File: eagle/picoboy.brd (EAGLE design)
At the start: 72 x 114.5 mm, 9 parts

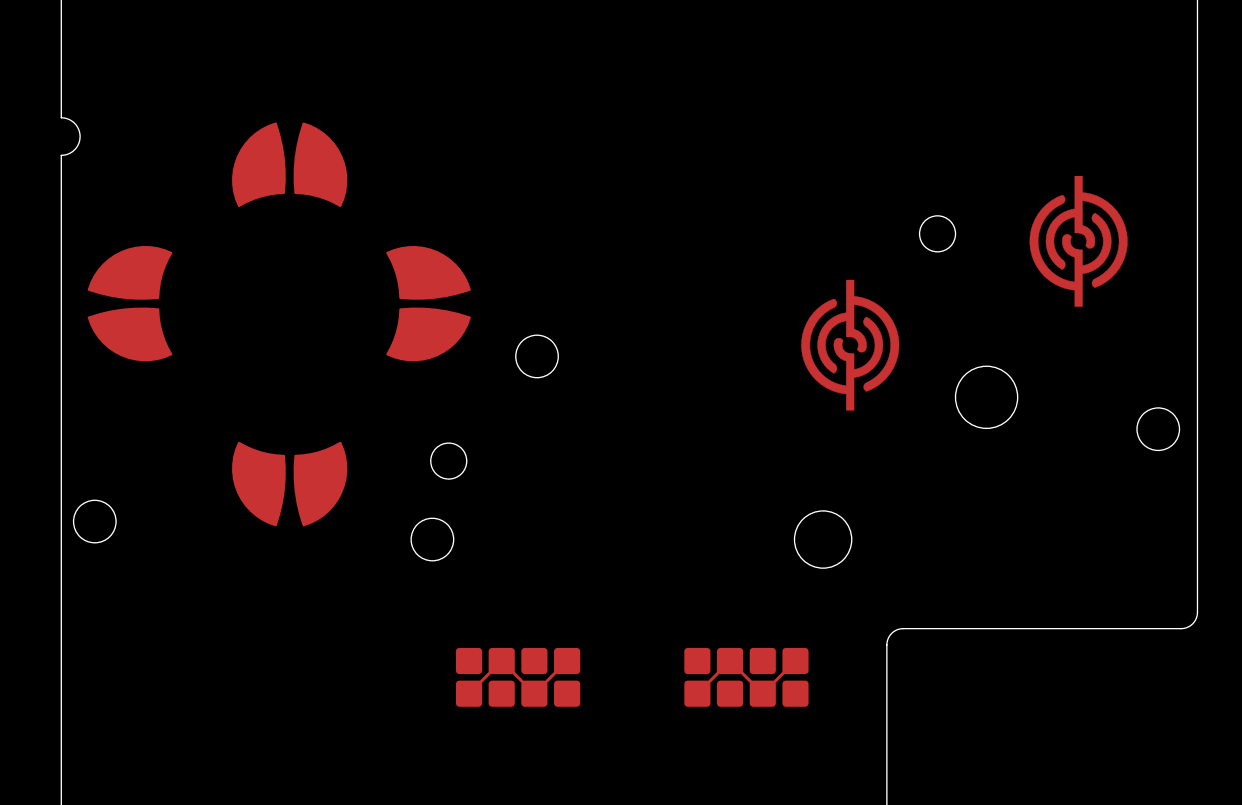
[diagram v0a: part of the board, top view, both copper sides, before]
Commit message: Update buttons possition on PCB
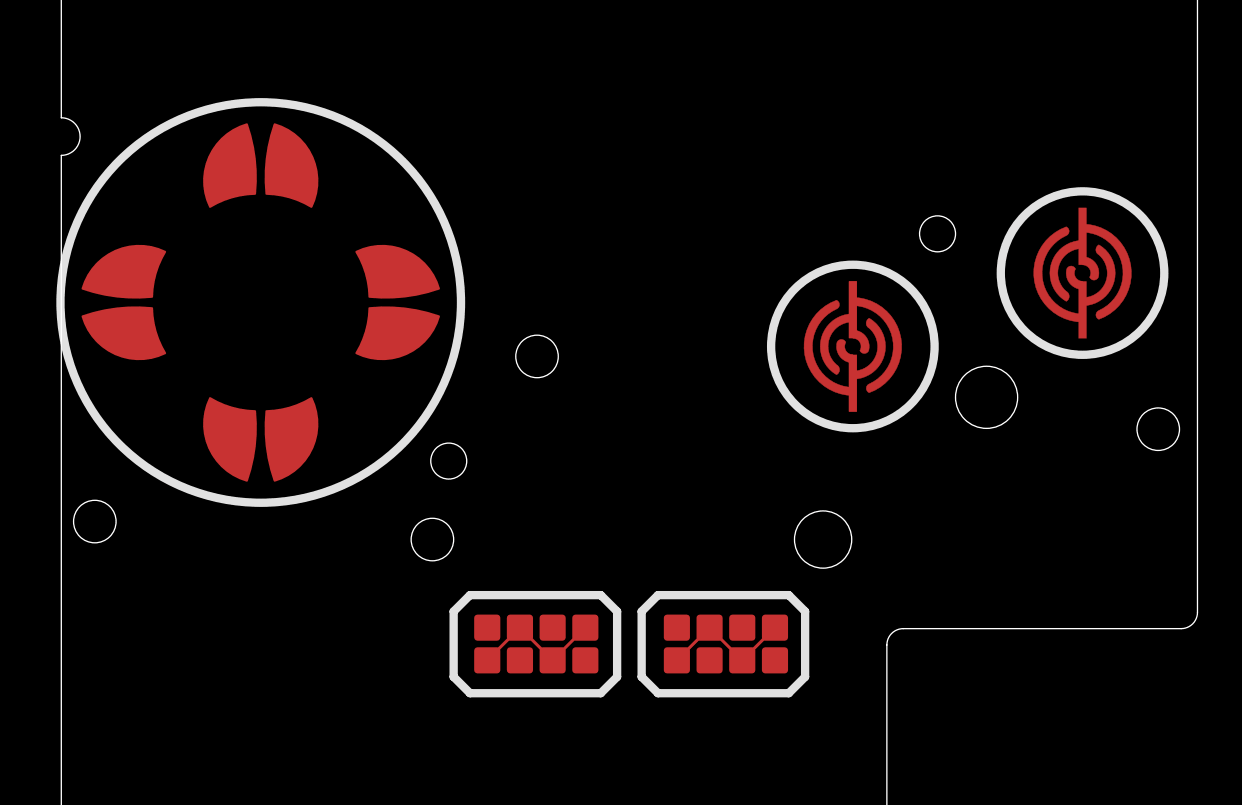
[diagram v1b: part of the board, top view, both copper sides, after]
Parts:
- moved DOWN 3.25 mm to (12.2, 29.4)
- moved START 2.40 mm to (40.7, 16.0)
- moved SELECT 2.32 mm to (29.1, 16.0)
- moved A 1.95 mm to (62.5, 38.7), turned to 180 degrees
- moved RIGHT 1.89 mm to (19.7, 36.9)
- moved UP 1.77 mm to (12.2, 44.4)
- moved LEFT 0.39 mm to (4.70, 36.9)
- moved B 0.18 mm to (48.4, 34.2), turned to 180 degrees
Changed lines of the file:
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@@
 <setting verticaltext="up"/>
 </settings>
-<grid distance="0.5" unitdist="mm" unit="mm" style="lines" multiple="1" display="no" altdistance="0.125" altunitdist="mm" altunit="mm"/>
+<grid distance="0.5" unitdist="mm" unit="mm" style="lines" multiple="1" display="yes" altdistance="0.125" altunitdist="mm" altunit="mm"/>
 <layers>
 <layer number="1" name="Top" color="4" fill="1" visible="yes" active="yes"/>
@@
 <board>
 <plain>
+<circle x="12.2" y="36.9" radius="12.25" width="0.508" layer="21"/>
+<circle x="48.42" y="34.21" radius="5" width="0.508" layer="21"/>
+<circle x="62.47" y="38.7" radius="5" width="0.508" layer="21"/>
+<wire x1="25" y1="19" x2="33" y2="19" width="0.508" layer="21"/>
+<wire x1="33" y1="19" x2="34" y2="18" width="0.508" layer="21"/>
+<wire x1="34" y1="18" x2="34" y2="14" width="0.508" layer="21"/>
+<wire x1="34" y1="14" x2="33" y2="13" width="0.508" layer="21"/>
+<wire x1="33" y1="13" x2="25" y2="13" width="0.508" layer="21"/>
+<wire x1="25" y1="13" x2="24" y2="14" width="0.508" layer="21"/>
+<wire x1="24" y1="14" x2="24" y2="18" width="0.508" layer="21"/>
+<wire x1="24" y1="18" x2="25" y2="19" width="0.508" layer="21"/>
+<wire x1="36.5" y1="19" x2="44.5" y2="19" width="0.508" layer="21"/>
+<wire x1="44.5" y1="19" x2="45.5" y2="18" width="0.508" layer="21"/>
+<wire x1="45.5" y1="18" x2="45.5" y2="14" width="0.508" layer="21"/>
+<wire x1="45.5" y1="14" x2="44.5" y2="13" width="0.508" layer="21"/>
+<wire x1="44.5" y1="13" x2="36.5" y2="13" width="0.508" layer="21"/>
+<wire x1="36.5" y1="13" x2="35.5" y2="14" width="0.508" layer="21"/>
+<wire x1="35.5" y1="14" x2="35.5" y2="18" width="0.508" layer="21"/>
+<wire x1="35.5" y1="18" x2="36.5" y2="19" width="0.508" layer="21"/>
 </plain>
 <attributes>
@@
 </autorouter>
 <elements>
-<element name="UP" library="GabozeLite" package="RETROESP32_CONDUCTIVE_BUTTON_DIRECTIONAL_THICK" value="RETROESP32_CONDUCTIVE_BUTTONCONDUCTIVE_BUTTON_DIRECTIONAL_THICK" x="13.97" y="44.45" smashed="yes" rot="R270"/>
-<element name="RIGHT" library="GabozeLite" package="RETROESP32_CONDUCTIVE_BUTTON_DIRECTIONAL_THICK" value="RETROESP32_CONDUCTIVE_BUTTONCONDUCTIVE_BUTTON_DIRECTIONAL_THICK" x="21.59" y="36.83" smashed="yes" rot="R180"/>
-<element name="DOWN" library="GabozeLite" package="RETROESP32_CONDUCTIVE_BUTTON_DIRECTIONAL_THICK" value="RETROESP32_CONDUCTIVE_BUTTONCONDUCTIVE_BUTTON_DIRECTIONAL_THICK" x="13.97" y="26.67" smashed="yes" rot="R90"/>
-<element name="LEFT" library="GabozeLite" package="RETROESP32_CONDUCTIVE_BUTTON_DIRECTIONAL_THICK" value="RETROESP32_CONDUCTIVE_BUTTONCONDUCTIVE_BUTTON_DIRECTIONAL_THICK" x="5.08" y="36.83" smashed="yes"/>
+<element name="UP" library="GabozeLite" package="RETROESP32_CONDUCTIVE_BUTTON_DIRECTIONAL_THICK" value="RETROESP32_CONDUCTIVE_BUTTONCONDUCTIVE_BUTTON_DIRECTIONAL_THICK" x="12.2" y="44.4" smashed="yes" rot="R270"/>
+<element name="RIGHT" library="GabozeLite" package="RETROESP32_CONDUCTIVE_BUTTON_DIRECTIONAL_THICK" value="RETROESP32_CONDUCTIVE_BUTTONCONDUCTIVE_BUTTON_DIRECTIONAL_THICK" x="19.7" y="36.9" smashed="yes" rot="R180"/>
+<element name="DOWN" library="GabozeLite" package="RETROESP32_CONDUCTIVE_BUTTON_DIRECTIONAL_THICK" value="RETROESP32_CONDUCTIVE_BUTTONCONDUCTIVE_BUTTON_DIRECTIONAL_THICK" x="12.2" y="29.4" smashed="yes" rot="R90"/>
+<element name="LEFT" library="GabozeLite" package="RETROESP32_CONDUCTIVE_BUTTON_DIRECTIONAL_THICK" value="RETROESP32_CONDUCTIVE_BUTTONCONDUCTIVE_BUTTON_DIRECTIONAL_THICK" x="4.7" y="36.9" smashed="yes"/>
 <element name="U$5" library="GabozeLite" package="RETROESP32_MGB-001" value="" x="0" y="0" smashed="yes"/>
-<element name="B" library="GabozeLite" package="RETROESP32_CONDUCTIVE_BUTTON_THICK" value="RETROESP32_CONDUCTIVE_BUTTONCONDUCTIVE_BUTTON_THICK" x="48.26" y="34.29" smashed="yes"/>
-<element name="A" library="GabozeLite" package="RETROESP32_CONDUCTIVE_BUTTON_THICK" value="RETROESP32_CONDUCTIVE_BUTTONCONDUCTIVE_BUTTON_THICK" x="62.23" y="40.64" smashed="yes"/>
-<element name="SELECT" library="GabozeLite" package="RETROESP32_CONDUCTIVE_BUTTON_THICK_STARTSELECT" value="RETROESP32_CONDUCTIVE_BUTTON_STARTSELECTCONDUCTIVE_BUTTON_THICK_STARTSELECT" x="27.94" y="13.97" smashed="yes"/>
-<element name="START" library="GabozeLite" package="RETROESP32_CONDUCTIVE_BUTTON_THICK_STARTSELECT" value="RETROESP32_CONDUCTIVE_BUTTON_STARTSELECTCONDUCTIVE_BUTTON_THICK_STARTSELECT" x="41.91" y="13.97" smashed="yes"/>
+<element name="B" library="GabozeLite" package="RETROESP32_CONDUCTIVE_BUTTON_THICK" value="RETROESP32_CONDUCTIVE_BUTTONCONDUCTIVE_BUTTON_THICK" x="48.42" y="34.21" smashed="yes" rot="R180"/>
+<element name="A" library="GabozeLite" package="RETROESP32_CONDUCTIVE_BUTTON_THICK" value="RETROESP32_CONDUCTIVE_BUTTONCONDUCTIVE_BUTTON_THICK" x="62.47" y="38.7" smashed="yes" rot="R180"/>
+<element name="SELECT" library="GabozeLite" package="RETROESP32_CONDUCTIVE_BUTTON_THICK_STARTSELECT" value="RETROESP32_CONDUCTIVE_BUTTON_STARTSELECTCONDUCTIVE_BUTTON_THICK_STARTSELECT" x="29.055" y="16.01" smashed="yes"/>
+<element name="START" library="GabozeLite" package="RETROESP32_CONDUCTIVE_BUTTON_THICK_STARTSELECT" value="RETROESP32_CONDUCTIVE_BUTTON_STARTSELECTCONDUCTIVE_BUTTON_THICK_STARTSELECT" x="40.655" y="16.01" smashed="yes"/>
 </elements>
 <signals>

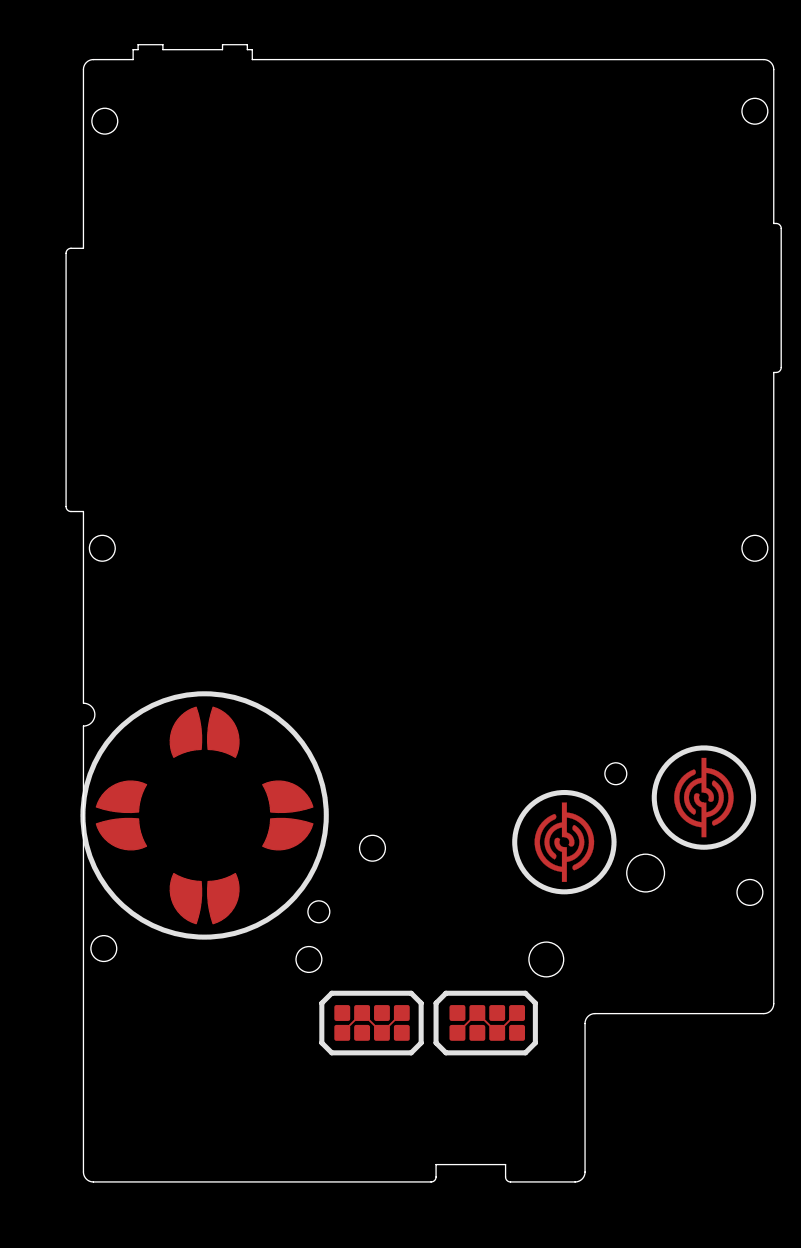
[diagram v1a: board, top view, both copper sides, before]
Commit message: Replace Game Boy Pocket with Game Boy Color PCB outline
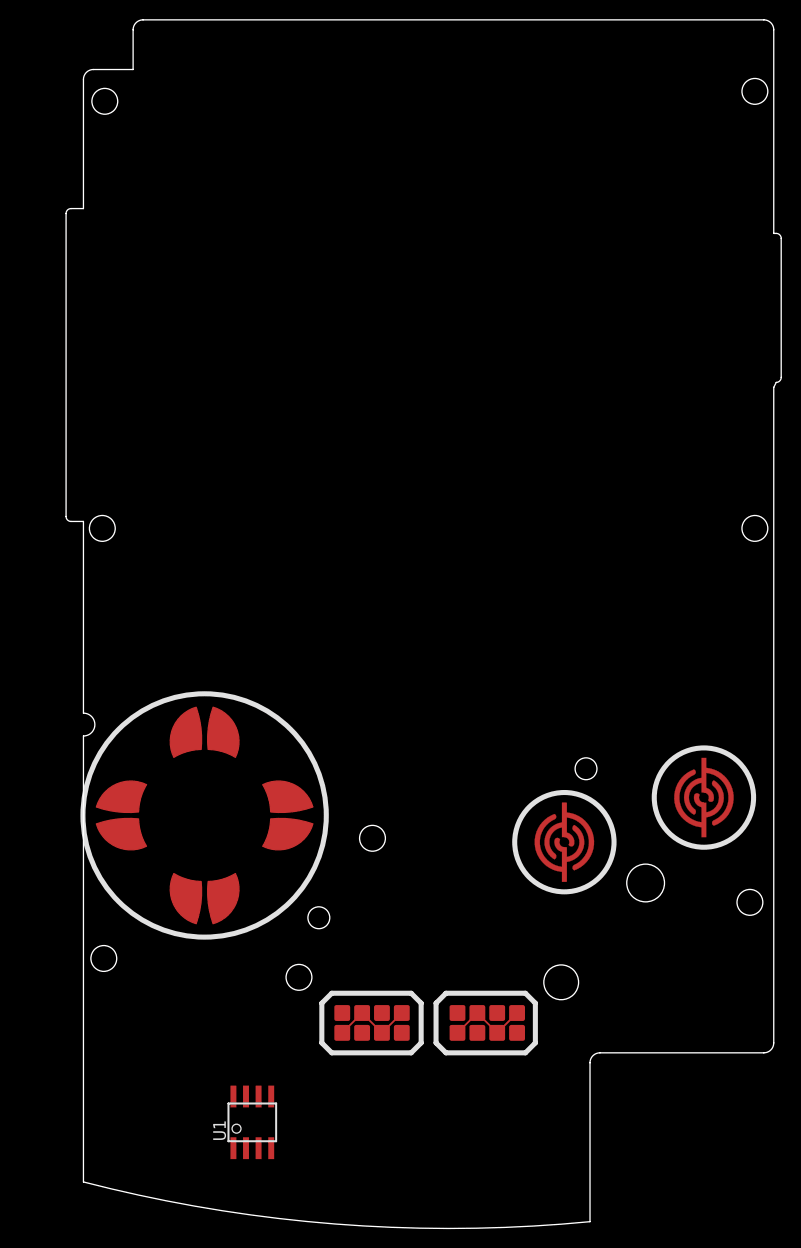
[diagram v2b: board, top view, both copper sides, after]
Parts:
- removed U$5: (no value), GabozeLite:RETROESP32_MGB-001
- added U$1: (no value), picoboy:PICOBOY_GBC_BOARD_OUTLINE
- added U1: RETROESP32_LM4875, GabozeLite:RETROESP32_SOIC8
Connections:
- new net GND: U1.6
- new net VDD: U1.1
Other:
- board size 72 x 114.5 mm -> 72 x 121.7 mm
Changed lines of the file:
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@@
 <element name="DOWN" library="GabozeLite" package="RETROESP32_CONDUCTIVE_BUTTON_DIRECTIONAL_THICK" value="RETROESP32_CONDUCTIVE_BUTTONCONDUCTIVE_BUTTON_DIRECTIONAL_THICK" x="12.2" y="29.4" smashed="yes" rot="R90"/>
 <element name="LEFT" library="GabozeLite" package="RETROESP32_CONDUCTIVE_BUTTON_DIRECTIONAL_THICK" value="RETROESP32_CONDUCTIVE_BUTTONCONDUCTIVE_BUTTON_DIRECTIONAL_THICK" x="4.7" y="36.9" smashed="yes"/>
-<element name="U$5" library="GabozeLite" package="RETROESP32_MGB-001" value="" x="0" y="0" smashed="yes"/>
 <element name="B" library="GabozeLite" package="RETROESP32_CONDUCTIVE_BUTTON_THICK" value="RETROESP32_CONDUCTIVE_BUTTONCONDUCTIVE_BUTTON_THICK" x="48.42" y="34.21" smashed="yes" rot="R180"/>
 <element name="A" library="GabozeLite" package="RETROESP32_CONDUCTIVE_BUTTON_THICK" value="RETROESP32_CONDUCTIVE_BUTTONCONDUCTIVE_BUTTON_THICK" x="62.47" y="38.7" smashed="yes" rot="R180"/>
 <element name="SELECT" library="GabozeLite" package="RETROESP32_CONDUCTIVE_BUTTON_THICK_STARTSELECT" value="RETROESP32_CONDUCTIVE_BUTTON_STARTSELECTCONDUCTIVE_BUTTON_THICK_STARTSELECT" x="29.055" y="16.01" smashed="yes"/>
 <element name="START" library="GabozeLite" package="RETROESP32_CONDUCTIVE_BUTTON_THICK_STARTSELECT" value="RETROESP32_CONDUCTIVE_BUTTON_STARTSELECTCONDUCTIVE_BUTTON_THICK_STARTSELECT" x="40.655" y="16.01" smashed="yes"/>
+<element name="U1" library="GabozeLite" package="RETROESP32_SOIC8" value="RETROESP32_LM4875" x="17" y="6" smashed="yes">
+<attribute name="NAME" x="14.333" y="4.095" size="1.27" layer="25" rot="R90"/>
+<attribute name="VALUE" x="20.937" y="4.095" size="1.27" layer="27" rot="R90"/>
+</element>
+<element name="U$1" library="picoboy" package="PICOBOY_GBC_BOARD_OUTLINE" value="" x="0" y="0" smashed="yes"/>
 </elements>
 <signals>
+<signal name="GND">
+<contactref element="U1" pad="6"/>
+</signal>
+<signal name="VDD">
+<contactref element="U1" pad="1"/>
+</signal>
 </signals>
 <mfgpreviewcolors>
